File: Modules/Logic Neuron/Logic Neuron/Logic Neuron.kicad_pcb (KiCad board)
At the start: 2 copper layers, 123.1 x 128.5 mm, 116 parts, among them J1 PJ301M-12, J10 PJ301M-12, J11 EURO_PWR_2x5, J2 PJ301M-12, J3 PJ301M-12, J4 PJ301M-12, J5 Conn_01x04, J6 Conn_01x04, J7 PJ301M-12, J8 PJ301M-12, J9 PJ301M-12, U1 TL074, U2 LM339, U3 TL074, U4 TL074, U9 LM339

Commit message: Logic Neuron Panel Design
Logic Neuron panel PCB designed, plus a little of the control plate.

to do next:
Add channel 4 indicator LED to the schematic
Divide the schematic into front panel and rear panel components
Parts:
- removed the REF** at (4.05, 95.2)
- removed the REF** at (4.25, 101.8)
- removed the Ref** at (-21.4, 143.9)
- removed the Ref** at (-25.0, 83.3)
- removed the Ref** at (-25.0, 59.5)
- removed the Ref** at (-8.00, 131.8)
- removed the Ref** at (-20.6, 131.7)
- removed the Ref** at (-7.40, 142.9)
- removed the Ref** at (-35.5, 143.6)
- removed the Ref** at (-49.5, 144.6)
- removed the Ref** at (-36.1, 132.4)
- removed the Ref** at (-48.8, 132.3)
- added REF**: Eurorack LED hole with ring, Eurocad:Eurorack_LED_hole_with_ring, F.Cu at (52.9, 101.5)
- added REF**: Eurorack LED hole with ring, Eurocad:Eurorack_LED_hole_with_ring, F.Cu at (52.9, 96.1)
- added REF**: Eurorack LED hole with ring, Eurocad:Eurorack_LED_hole_with_ring, F.Cu at (52.9, 90.7)
- added Ref**: Eurorack jack hole, Eurocad:Eurorack_jack_hole, F.Cu at (21.8, 127.8)
- added Ref**: Eurorack jack hole, Eurocad:Eurorack_jack_hole, F.Cu at (52.6, 114.2)
- added Ref**: Pothole_Davies1900H_white, Eurocad:Pothole_Davies1900H_white, F.Cu at (37.1, 58.5)
- added Ref**: Pothole_Davies1900H_white, Eurocad:Pothole_Davies1900H_white, F.Cu at (37.1, 77.3)
- added Ref**: Eurorack jack hole, Eurocad:Eurorack_jack_hole, F.Cu at (32.1, 114.2)
- added Ref**: Eurorack jack hole, Eurocad:Eurorack_jack_hole, F.Cu at (42.3, 127.7)
- added Ref**: Eurorack jack hole, Eurocad:Eurorack_jack_hole, F.Cu at (32.1, 127.7)
- added Ref**: Eurorack jack hole, Eurocad:Eurorack_jack_hole, F.Cu at (52.6, 127.7)
- added Ref**: Eurorack jack hole, Eurocad:Eurorack_jack_hole, F.Cu at (21.8, 114.2)
- added Ref**: Eurorack jack hole, Eurocad:Eurorack_jack_hole, F.Cu at (42.3, 114.2)
- moved J4 232.9 mm to (73.2, 127.7), turned to 180 degrees
- moved RV2 231.4 mm to (78.3, 39.7)
- moved J1 222.7 mm to (62.9, 114.2), turned to 180 degrees
- moved RV5 217.3 mm to (78.3, 96.2)
- moved RV3 211.9 mm to (78.3, 58.5)
- moved J2 207.7 mm to (62.9, 127.7), turned to 180 degrees
- moved J10 201.9 mm to (93.8, 127.7), turned to 180 degrees
- moved J9 200.0 mm to (93.8, 114.2), turned to 180 degrees
- moved RV4 193.2 mm to (78.3, 77.3)
- moved J3 189.0 mm to (73.2, 114.2), turned to 180 degrees
- moved J7 181.6 mm to (83.5, 127.7), turned to 180 degrees
- moved J8 172.9 mm to (83.5, 114.2), turned to 180 degrees
- moved REF** 73.2 mm to (22.6, 77.3)
- moved REF** 72.3 mm to (22.6, 39.8)
- moved REF** 71.8 mm to (22.6, 58.5)
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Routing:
- added copper zone on B.Cu, net GND
- added copper zone on F.Cu, net GND
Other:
- outline, holes or cut-outs redrawn
- net class Default removed
- board text added: "-1"
- board text added: "-2"
- board text added: "-3"
- board text added: "0"
- board text added: "1"
- board text added: "2"
- board text added: "3"
- board text added: "4"
- board text added: "SUM"
- board text added: "SUM T"
- board text added: "THRESH"

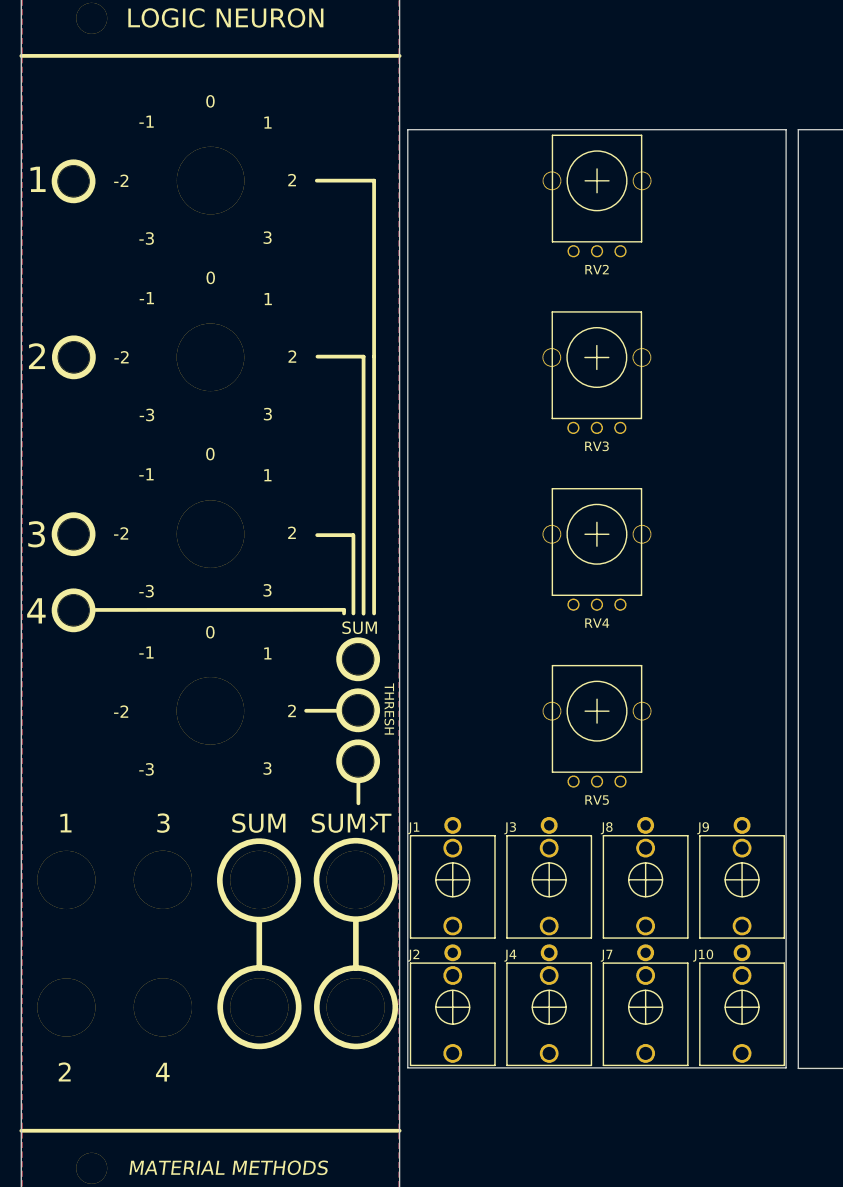
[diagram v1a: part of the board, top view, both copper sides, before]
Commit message: Logic Neuron : increased spacing between pots and jacks
Expanded control board from 100mm high to 110mm to allow more finger space between knobs and jacks.
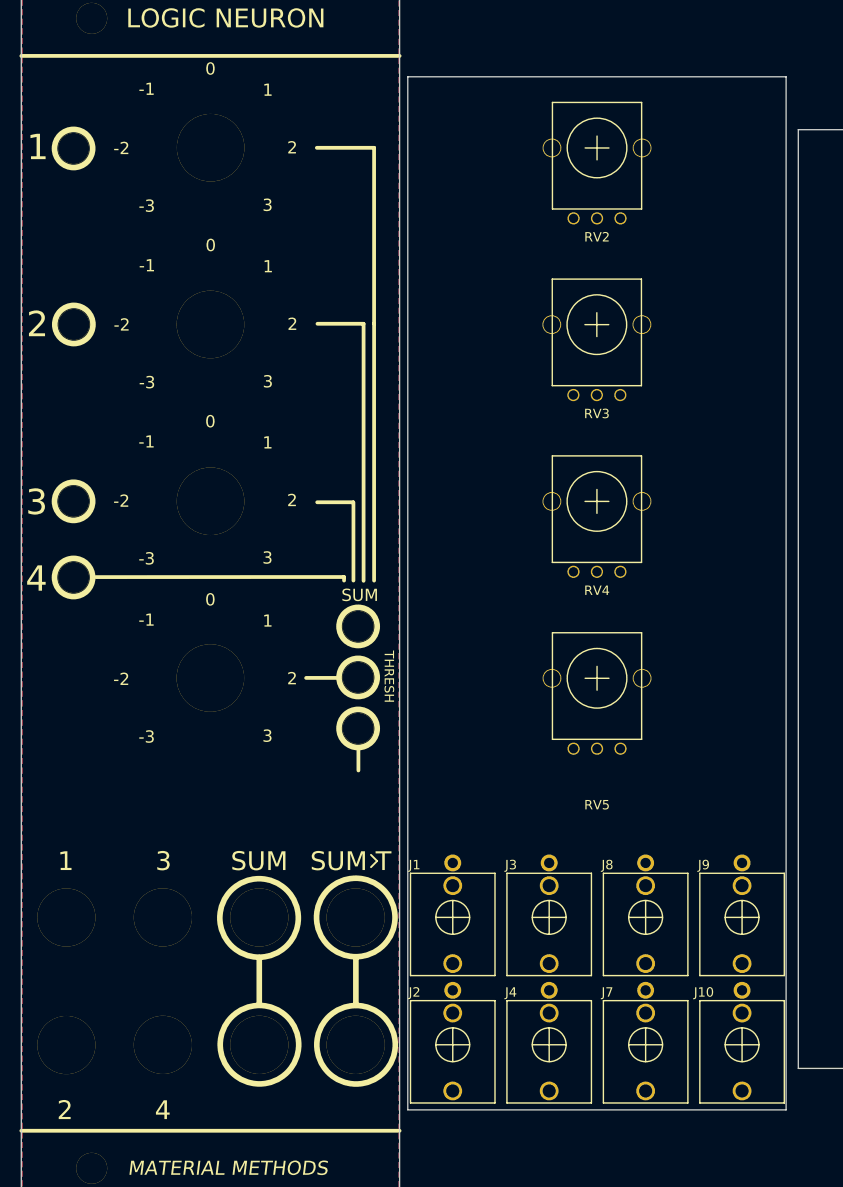
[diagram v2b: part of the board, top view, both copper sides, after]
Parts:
- moved Ref** 4.00 mm to (42.3, 131.7)
- moved Ref** 4.00 mm to (32.1, 131.7)
- moved Ref** 4.00 mm to (52.6, 131.7)
- moved J1 4.00 mm to (62.9, 118.2)
- moved J3 4.00 mm to (73.2, 118.2)
- moved J8 4.00 mm to (83.5, 118.2)
- moved J9 4.00 mm to (93.8, 118.2)
- moved Ref** 4.00 mm to (52.6, 118.2)
- moved Ref** 4.00 mm to (32.1, 118.2)
- moved Ref** 4.00 mm to (21.8, 118.2)
- moved Ref** 4.00 mm to (42.3, 118.2)
- moved J10 4.00 mm to (93.8, 131.7)
- moved J2 4.00 mm to (62.9, 131.7)
- moved J4 4.00 mm to (73.2, 131.7)
- moved J7 4.00 mm to (83.5, 131.7)
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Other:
- outline, holes or cut-outs redrawn

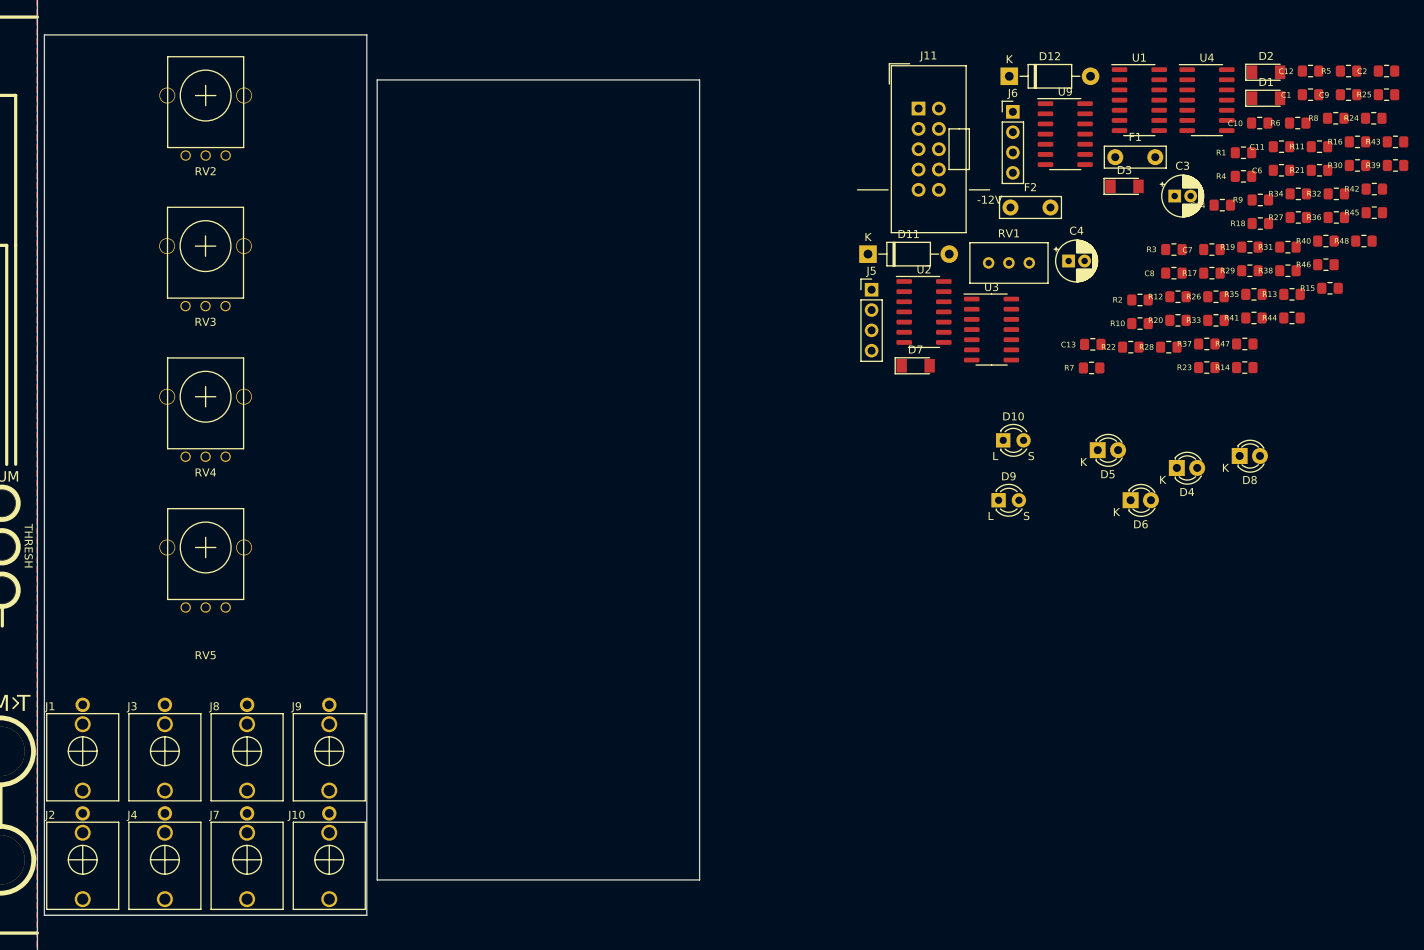
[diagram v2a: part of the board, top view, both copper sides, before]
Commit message: Logic Neuron
Logic Neuron:
- Added LED indicator for input 4
- updated some footprints that were broken in the Kicad update
- started laying out the control board
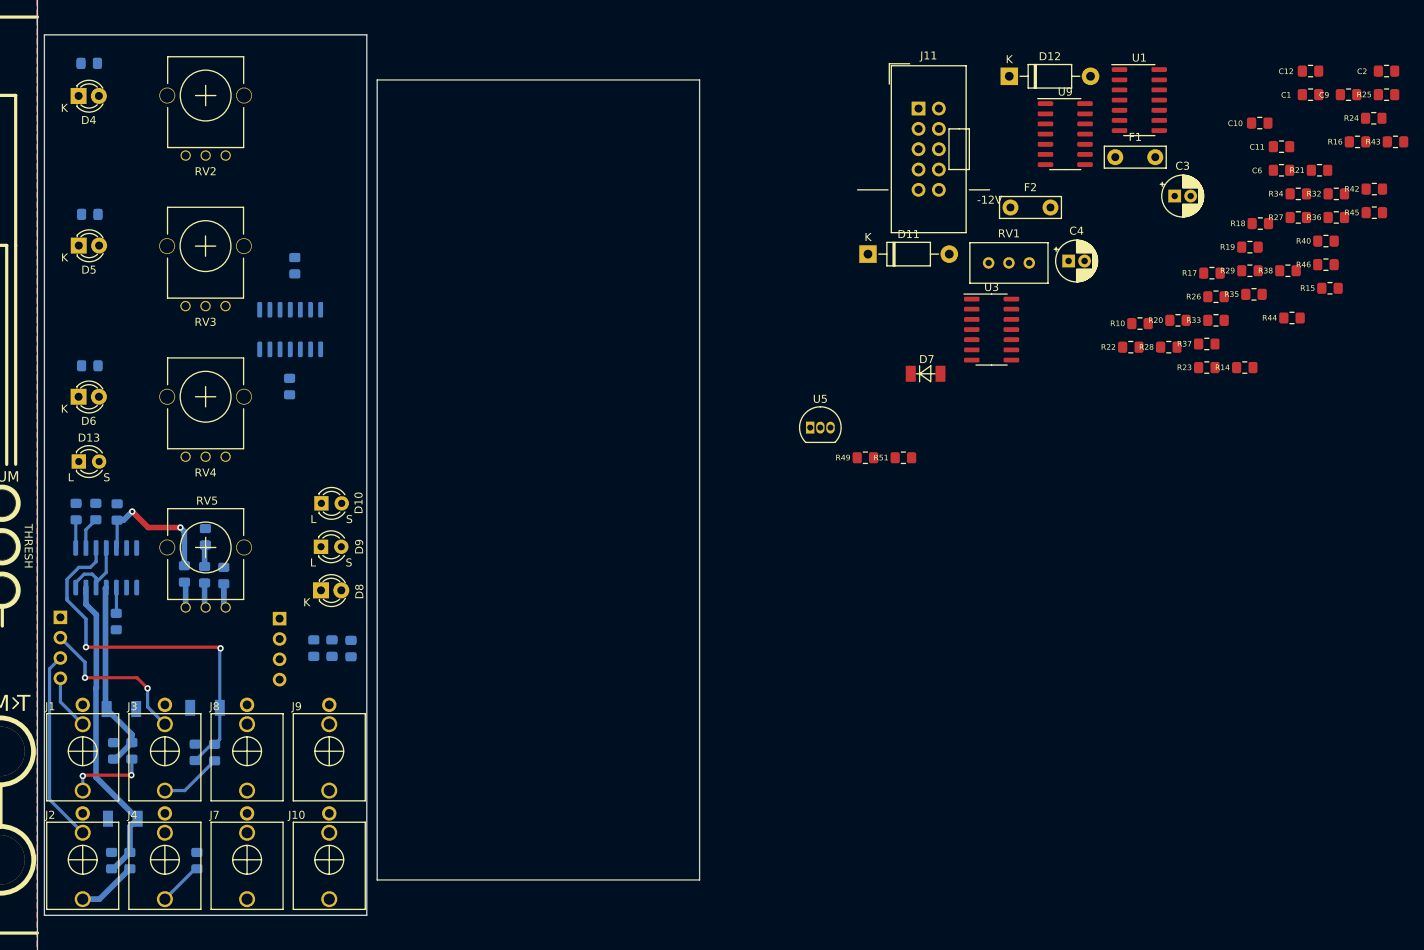
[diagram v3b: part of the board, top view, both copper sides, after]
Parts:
- added D13: LED_Bicolor_Tayda_A-1076, Eurocad:TaydaA-1076_bicolor_LED, F.Cu at (62.5, 82.0)
- added R49: 100k, Eurocad:R_0805_2012Metric_Pad1.15x1.40mm_HandSolder_smallText, F.Cu at (160.8, 81.5)
- added R50: 660R, Eurocad:R_0805_2012Metric_Pad1.15x1.40mm_HandSolder_smallText, B.Cu at (96.5, 105.3)
- added R51: 100k, Eurocad:R_0805_2012Metric_Pad1.15x1.40mm_HandSolder_smallText, F.Cu at (165.5, 81.5)
- added U5: LM79L05_TO92, Package_TO_SOT_THT:TO-92_Inline, F.Cu at (153.9, 77.7)
- C13, C14, C7, C8, J5, J6, R1, R11, R12, R13, R2, R3, R30, R31, R39, R4, R41, R47, R48, R5, R6, R7, R8, R9, U2, U4: moved to B.Cu
- D1, D2, D3: footprint Diode_SMD:D_MiniMELF -> Eurocad:LL4148_sam; moved to B.Cu
- D7: footprint Diode_SMD:D_MiniMELF -> Eurocad:LL4148_sam
- moved R5 176.2 mm to (66.8, 118.1), turned to -90 degrees
- moved R6 174.6 mm to (66.5, 131.8), turned to -90 degrees
- moved D2 169.1 mm to (69.2, 125.6), turned to 180 degrees
- moved R8 165.0 mm to (62.1, 88.2), turned to -90 degrees
- moved D1 163.8 mm to (66.5, 113.9)
- moved R1 157.8 mm to (69.1, 118.1), turned to -90 degrees
- moved R4 156.3 mm to (77.2, 131.8), turned to 90 degrees
- moved R11 154.1 mm to (63.8, 32.2), turned to 180 degrees
- moved R30 150.7 mm to (80.6, 96.2), turned to -90 degrees
- moved R13 150.5 mm to (63.8, 70.0), turned to 180 degrees
- moved R9 150.0 mm to (77.0, 118.3), turned to -90 degrees
- moved R48 149.5 mm to (78.3, 91.3), turned to 90 degrees
- moved R39 148.1 mm to (91.8, 105.3), turned to -90 degrees
- moved D4 144.9 mm to (63.7, 36.2)
- moved C7 144.6 mm to (67.1, 102.0), turned to 90 degrees
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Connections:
- net Net-(D10-Pad2) renamed /LED_SUM
- net Net-(D9-Pad2) renamed /LED_threshold
- J10 pad 2: (no net) -> unconnected-(J10-Pad2)
- J7 pad 2: (no net) -> unconnected-(J7-Pad2)
- J8 pad 2: (no net) -> unconnected-(J8-Pad2)
- J9 pad 2: (no net) -> unconnected-(J9-Pad2)
- U2 pad 14: (no net) -> unconnected-(U2-Pad14)
- U4 pad 10: GND -> Net-(U4-Pad10)
- U4 pad 8: Net-(U4-Pad8) -> /LED_in4
- U4 pad 9: Net-(U4-Pad8) -> Net-(U4-Pad9)
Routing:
- net Net-(D3-Pad1): track 0.00 -> 48.2 mm, vias 0 -> 2
- net Net-(D2-Pad1): track 0.00 -> 39.4 mm
- net norm_in2: track 0.00 -> 24.1 mm
- net Net-(D1-Pad1): track 0.00 -> 23.9 mm
- net norm_in3: track 0.00 -> 20.0 mm, vias 0 -> 2
- net -5V_regulated: track 0.00 -> 17.7 mm, vias 0 -> 2
- net V_threshold: track 0.00 -> 10.5 mm
- net in1: track 0.00 -> 10.3 mm, vias 0 -> 2
- net in3: track 0.00 -> 7.76 mm
- net in2: track 0.00 -> 7.47 mm
- net norm_in1: track 0.00 -> 6.89 mm
- net Net-(J4-Pad3): track 0.00 -> 5.58 mm
- net Net-(R7-Pad2): track 0.00 -> 4.66 mm
- net Net-(R8-Pad2): track 0.00 -> 3.54 mm
- net +12V: track 0.00 -> 3.23 mm
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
